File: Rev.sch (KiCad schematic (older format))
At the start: 17 parts

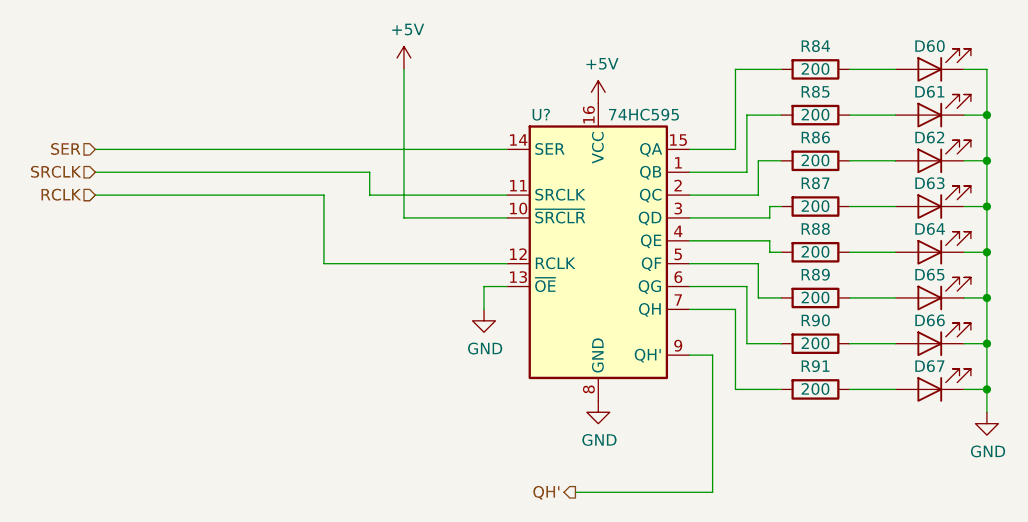
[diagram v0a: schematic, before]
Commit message: footprints; library for 7seg; start pcb layout
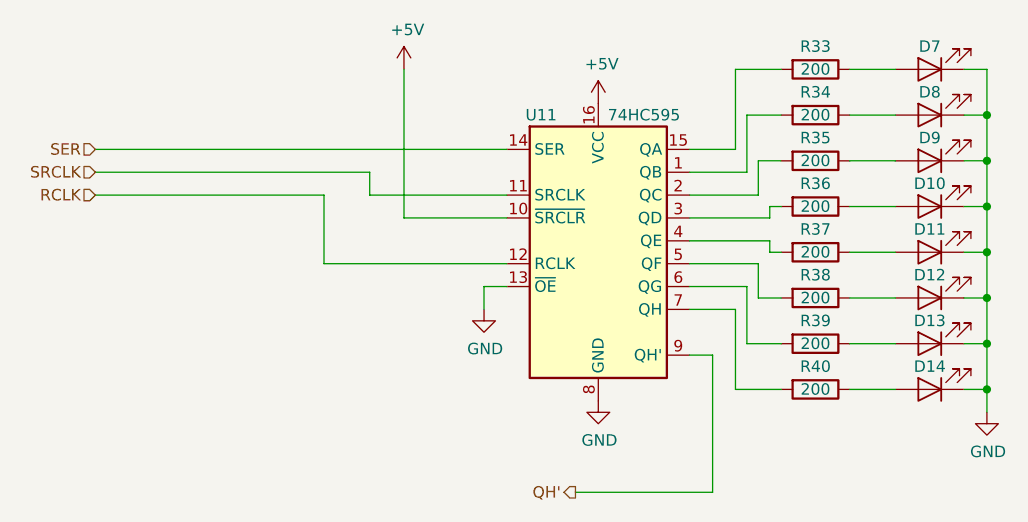
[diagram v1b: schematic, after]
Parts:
- D10: renamed from D63; footprint (none) -> LED_THT:LED_D3.0mm_Clear
- D11: renamed from D64; footprint (none) -> LED_THT:LED_D3.0mm_Clear
- D12: renamed from D65; footprint (none) -> LED_THT:LED_D3.0mm_Clear
- D13: renamed from D66; footprint (none) -> LED_THT:LED_D3.0mm_Clear
- D14: renamed from D67; footprint (none) -> LED_THT:LED_D3.0mm_Clear
- D7: renamed from D60; footprint (none) -> LED_THT:LED_D3.0mm_Clear
- D8: renamed from D61; footprint (none) -> LED_THT:LED_D3.0mm_Clear
- D9: renamed from D62; footprint (none) -> LED_THT:LED_D3.0mm_Clear
- R33: renamed from R84; footprint (none) -> Resistor_SMD:R_0603_1608Metric
- R34: renamed from R85; footprint (none) -> Resistor_SMD:R_0603_1608Metric
- R35: renamed from R86; footprint (none) -> Resistor_SMD:R_0603_1608Metric
- R36: renamed from R87; footprint (none) -> Resistor_SMD:R_0603_1608Metric
- R37: renamed from R88; footprint (none) -> Resistor_SMD:R_0603_1608Metric
- R38: renamed from R89; footprint (none) -> Resistor_SMD:R_0603_1608Metric
- R39: renamed from R90; footprint (none) -> Resistor_SMD:R_0603_1608Metric
- R40: renamed from R91; footprint (none) -> Resistor_SMD:R_0603_1608Metric
- U11: renamed from U?; footprint (none) -> Package_SO:SOIC-16_3.9x9.9mm_P1.27mm
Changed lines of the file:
@@
 $Descr A4 11693 8268
 encoding utf-8
-Sheet 7 9
+Sheet 6 9
 Title ""
 Date ""
@@
 AR Path="/61F6E690" Ref="U?"  Part="1"
 AR Path="/5FCC310D/61F6E690" Ref="U?"  Part="1"
-AR Path="/61EF75E6/61F6E690" Ref="U?"  Part="1"
-F 0 "U?" H 5450 4150 50  0000 C CNN
+AR Path="/61EF75E6/61F6E690" Ref="U11"  Part="1"
+F 0 "U11" H 5450 4150 50  0000 C CNN
 F 1 "74HC595" H 5900 4150 50  0000 C CNN
-F 2 "" H 5700 3600 50  0001 C CNN
+F 2 "Package_SO:SOIC-16_3.9x9.9mm_P1.27mm" H 5700 3600 50  0001 C CNN
 F 3 "http://www.ti.com/lit/ds/symlink/sn74hc595.pdf" H 5700 3600 50  0001 C CNN
 	1    5700 3600
@@
 AR Path="/61F6E696" Ref="R?"  Part="1"
 AR Path="/5FCC310D/61F6E696" Ref="R?"  Part="1"
-AR Path="/61EF75E6/61F6E696" Ref="R84"  Part="1"
-F 0 "R84" V 6550 2850 50  0000 C CNN
+AR Path="/61EF75E6/61F6E696" Ref="R33"  Part="1"
+F 0 "R33" V 6550 2850 50  0000 C CNN
 F 1 "200" V 6650 2850 50  0000 C CNN
-F 2 "" V 6580 2850 50  0001 C CNN
+F 2 "Resistor_SMD:R_0603_1608Metric" V 6580 2850 50  0001 C CNN
 F 3 "~" H 6650 2850 50  0001 C CNN
 	1    6650 2850
@@
 AR Path="/61F6E69C" Ref="D?"  Part="1"
 AR Path="/5FCC310D/61F6E69C" Ref="D?"  Part="1"
-AR Path="/61EF75E6/61F6E69C" Ref="D60"  Part="1"
-F 0 "D60" H 7150 2750 50  0000 C CNN
+AR Path="/61EF75E6/61F6E69C" Ref="D7"  Part="1"
+F 0 "D7" H 7150 2750 50  0000 C CNN
 F 1 "LED" H 7142 2686 50  0001 C CNN
-F 2 "" H 7150 2850 50  0001 C CNN
+F 2 "LED_THT:LED_D3.0mm_Clear" H 7150 2850 50  0001 C CNN
 F 3 "~" H 7150 2850 50  0001 C CNN
 	1    7150 2850
@@
 AR Path="/61F6E6A2" Ref="R?"  Part="1"
 AR Path="/5FCC310D/61F6E6A2" Ref="R?"  Part="1"
-AR Path="/61EF75E6/61F6E6A2" Ref="R85"  Part="1"
-F 0 "R85" V 6550 3050 50  0000 C CNN
+AR Path="/61EF75E6/61F6E6A2" Ref="R34"  Part="1"
+F 0 "R34" V 6550 3050 50  0000 C CNN
 F 1 "200" V 6650 3050 50  0000 C CNN
-F 2 "" V 6580 3050 50  0001 C CNN
+F 2 "Resistor_SMD:R_0603_1608Metric" V 6580 3050 50  0001 C CNN
 F 3 "~" H 6650 3050 50  0001 C CNN
 	1    6650 3050
@@
 AR Path="/61F6E6A8" Ref="D?"  Part="1"
 AR Path="/5FCC310D/61F6E6A8" Ref="D?"  Part="1"
-AR Path="/61EF75E6/61F6E6A8" Ref="D61"  Part="1"
-F 0 "D61" H 7150 2950 50  0000 C CNN
+AR Path="/61EF75E6/61F6E6A8" Ref="D8"  Part="1"
+F 0 "D8" H 7150 2950 50  0000 C CNN
 F 1 "LED" H 7142 2886 50  0001 C CNN
-F 2 "" H 7150 3050 50  0001 C CNN
+F 2 "LED_THT:LED_D3.0mm_Clear" H 7150 3050 50  0001 C CNN
 F 3 "~" H 7150 3050 50  0001 C CNN
 	1    7150 3050
@@
 AR Path="/61F6E6AE" Ref="R?"  Part="1"
 AR Path="/5FCC310D/61F6E6AE" Ref="R?"  Part="1"
-AR Path="/61EF75E6/61F6E6AE" Ref="R86"  Part="1"
-F 0 "R86" V 6550 3250 50  0000 C CNN
+AR Path="/61EF75E6/61F6E6AE" Ref="R35"  Part="1"
+F 0 "R35" V 6550 3250 50  0000 C CNN
 F 1 "200" V 6650 3250 50  0000 C CNN
-F 2 "" V 6580 3250 50  0001 C CNN
+F 2 "Resistor_SMD:R_0603_1608Metric" V 6580 3250 50  0001 C CNN
 F 3 "~" H 6650 3250 50  0001 C CNN
 	1    6650 3250
@@
 AR Path="/61F6E6B4" Ref="D?"  Part="1"
 AR Path="/5FCC310D/61F6E6B4" Ref="D?"  Part="1"
-AR Path="/61EF75E6/61F6E6B4" Ref="D62"  Part="1"
-F 0 "D62" H 7150 3150 50  0000 C CNN
+AR Path="/61EF75E6/61F6E6B4" Ref="D9"  Part="1"
+F 0 "D9" H 7150 3150 50  0000 C CNN
 F 1 "LED" H 7142 3086 50  0001 C CNN
-F 2 "" H 7150 3250 50  0001 C CNN
+F 2 "LED_THT:LED_D3.0mm_Clear" H 7150 3250 50  0001 C CNN
 F 3 "~" H 7150 3250 50  0001 C CNN
 	1    7150 3250
@@
 AR Path="/61F6E6BA" Ref="R?"  Part="1"
 AR Path="/5FCC310D/61F6E6BA" Ref="R?"  Part="1"
-AR Path="/61EF75E6/61F6E6BA" Ref="R87"  Part="1"
-F 0 "R87" V 6550 3450 50  0000 C CNN
+AR Path="/61EF75E6/61F6E6BA" Ref="R36"  Part="1"
+F 0 "R36" V 6550 3450 50  0000 C CNN
 F 1 "200" V 6650 3450 50  0000 C CNN
-F 2 "" V 6580 3450 50  0001 C CNN
+F 2 "Resistor_SMD:R_0603_1608Metric" V 6580 3450 50  0001 C CNN
 F 3 "~" H 6650 3450 50  0001 C CNN
 	1    6650 3450
@@
 AR Path="/61F6E6C0" Ref="D?"  Part="1"
 AR Path="/5FCC310D/61F6E6C0" Ref="D?"  Part="1"
-AR Path="/61EF75E6/61F6E6C0" Ref="D63"  Part="1"
-F 0 "D63" H 7150 3350 50  0000 C CNN
+AR Path="/61EF75E6/61F6E6C0" Ref="D10"  Part="1"
+F 0 "D10" H 7150 3350 50  0000 C CNN
 F 1 "LED" H 7142 3286 50  0001 C CNN
-F 2 "" H 7150 3450 50  0001 C CNN
+F 2 "LED_THT:LED_D3.0mm_Clear" H 7150 3450 50  0001 C CNN
 F 3 "~" H 7150 3450 50  0001 C CNN
 	1    7150 3450
@@
 AR Path="/61F6E6C6" Ref="R?"  Part="1"
 AR Path="/5FCC310D/61F6E6C6" Ref="R?"  Part="1"
-AR Path="/61EF75E6/61F6E6C6" Ref="R88"  Part="1"
-F 0 "R88" V 6550 3650 50  0000 C CNN
+AR Path="/61EF75E6/61F6E6C6" Ref="R37"  Part="1"
+F 0 "R37" V 6550 3650 50  0000 C CNN
 F 1 "200" V 6650 3650 50  0000 C CNN
-F 2 "" V 6580 3650 50  0001 C CNN
+F 2 "Resistor_SMD:R_0603_1608Metric" V 6580 3650 50  0001 C CNN
 F 3 "~" H 6650 3650 50  0001 C CNN
 	1    6650 3650
@@
 AR Path="/61F6E6CC" Ref="D?"  Part="1"
 AR Path="/5FCC310D/61F6E6CC" Ref="D?"  Part="1"
-AR Path="/61EF75E6/61F6E6CC" Ref="D64"  Part="1"
-F 0 "D64" H 7150 3550 50  0000 C CNN
+AR Path="/61EF75E6/61F6E6CC" Ref="D11"  Part="1"
+F 0 "D11" H 7150 3550 50  0000 C CNN
 F 1 "LED" H 7142 3486 50  0001 C CNN
-F 2 "" H 7150 3650 50  0001 C CNN
+F 2 "LED_THT:LED_D3.0mm_Clear" H 7150 3650 50  0001 C CNN
 F 3 "~" H 7150 3650 50  0001 C CNN
 	1    7150 3650
@@
 AR Path="/61F6E6D2" Ref="R?"  Part="1"
 AR Path="/5FCC310D/61F6E6D2" Ref="R?"  Part="1"
-AR Path="/61EF75E6/61F6E6D2" Ref="R89"  Part="1"
-F 0 "R89" V 6550 3850 50  0000 C CNN
+AR Path="/61EF75E6/61F6E6D2" Ref="R38"  Part="1"
+F 0 "R38" V 6550 3850 50  0000 C CNN
 F 1 "200" V 6650 3850 50  0000 C CNN
-F 2 "" V 6580 3850 50  0001 C CNN
+F 2 "Resistor_SMD:R_0603_1608Metric" V 6580 3850 50  0001 C CNN
 F 3 "~" H 6650 3850 50  0001 C CNN
 	1    6650 3850
@@
 AR Path="/61F6E6D8" Ref="D?"  Part="1"
 AR Path="/5FCC310D/61F6E6D8" Ref="D?"  Part="1"
-AR Path="/61EF75E6/61F6E6D8" Ref="D65"  Part="1"
-F 0 "D65" H 7150 3750 50  0000 C CNN
+AR Path="/61EF75E6/61F6E6D8" Ref="D12"  Part="1"
+F 0 "D12" H 7150 3750 50  0000 C CNN
 F 1 "LED" H 7142 3686 50  0001 C CNN
-F 2 "" H 7150 3850 50  0001 C CNN
+F 2 "LED_THT:LED_D3.0mm_Clear" H 7150 3850 50  0001 C CNN
 F 3 "~" H 7150 3850 50  0001 C CNN
 	1    7150 3850
@@
 AR Path="/61F6E6DE" Ref="R?"  Part="1"
 AR Path="/5FCC310D/61F6E6DE" Ref="R?"  Part="1"
-AR Path="/61EF75E6/61F6E6DE" Ref="R90"  Part="1"
-F 0 "R90" V 6550 4050 50  0000 C CNN
+AR Path="/61EF75E6/61F6E6DE" Ref="R39"  Part="1"
+F 0 "R39" V 6550 4050 50  0000 C CNN
 F 1 "200" V 6650 4050 50  0000 C CNN
-F 2 "" V 6580 4050 50  0001 C CNN
+F 2 "Resistor_SMD:R_0603_1608Metric" V 6580 4050 50  0001 C CNN
 F 3 "~" H 6650 4050 50  0001 C CNN
 	1    6650 4050
@@
 AR Path="/61F6E6E4" Ref="D?"  Part="1"
 AR Path="/5FCC310D/61F6E6E4" Ref="D?"  Part="1"
-AR Path="/61EF75E6/61F6E6E4" Ref="D66"  Part="1"
-F 0 "D66" H 7150 3950 50  0000 C CNN
+AR Path="/61EF75E6/61F6E6E4" Ref="D13"  Part="1"
+F 0 "D13" H 7150 3950 50  0000 C CNN
 F 1 "LED" H 7142 3886 50  0001 C CNN
-F 2 "" H 7150 4050 50  0001 C CNN
+F 2 "LED_THT:LED_D3.0mm_Clear" H 7150 4050 50  0001 C CNN
 F 3 "~" H 7150 4050 50  0001 C CNN
 	1    7150 4050
@@
 AR Path="/61F6E6EA" Ref="R?"  Part="1"
 AR Path="/5FCC310D/61F6E6EA" Ref="R?"  Part="1"
-AR Path="/61EF75E6/61F6E6EA" Ref="R91"  Part="1"
-F 0 "R91" V 6550 4250 50  0000 C CNN
+AR Path="/61EF75E6/61F6E6EA" Ref="R40"  Part="1"
+F 0 "R40" V 6550 4250 50  0000 C CNN
 F 1 "200" V 6650 4250 50  0000 C CNN
-F 2 "" V 6580 4250 50  0001 C CNN
+F 2 "Resistor_SMD:R_0603_1608Metric" V 6580 4250 50  0001 C CNN
 F 3 "~" H 6650 4250 50  0001 C CNN
 	1    6650 4250
@@
 AR Path="/61F6E6F0" Ref="D?"  Part="1"
 AR Path="/5FCC310D/61F6E6F0" Ref="D?"  Part="1"
-AR Path="/61EF75E6/61F6E6F0" Ref="D67"  Part="1"
-F 0 "D67" H 7150 4150 50  0000 C CNN
+AR Path="/61EF75E6/61F6E6F0" Ref="D14"  Part="1"
+F 0 "D14" H 7150 4150 50  0000 C CNN
 F 1 "LED" H 7150 4150 50  0001 C CNN
-F 2 "" H 7150 4250 50  0001 C CNN
+F 2 "LED_THT:LED_D3.0mm_Clear" H 7150 4250 50  0001 C CNN
 F 3 "~" H 7150 4250 50  0001 C CNN
 	1    7150 4250
@@
 AR Path="/61F6E72D" Ref="#PWR?"  Part="1"
 AR Path="/5FCC310D/61F6E72D" Ref="#PWR?"  Part="1"
-AR Path="/61EF75E6/61F6E72D" Ref="#PWR?"  Part="1"
-F 0 "#PWR?" H 7400 4100 50  0001 C CNN
+AR Path="/61EF75E6/61F6E72D" Ref="#PWR044"  Part="1"
+F 0 "#PWR044" H 7400 4100 50  0001 C CNN
 F 1 "GND" H 7405 4177 50  0000 C CNN
 F 2 "" H 7400 4350 50  0001 C CNN
@@
 AR Path="/61F6E735" Ref="#PWR?"  Part="1"
 AR Path="/5FCC310D/61F6E735" Ref="#PWR?"  Part="1"
-AR Path="/61EF75E6/61F6E735" Ref="#PWR?"  Part="1"
-F 0 "#PWR?" H 5700 2850 50  0001 C CNN
+AR Path="/61EF75E6/61F6E735" Ref="#PWR042"  Part="1"
+F 0 "#PWR042" H 5700 2850 50  0001 C CNN
 F 1 "+5V" H 5715 3173 50  0000 C CNN
 F 2 "" H 5700 3000 50  0001 C CNN
@@
 AR Path="/61F6E73B" Ref="#PWR?"  Part="1"
 AR Path="/5FCC310D/61F6E73B" Ref="#PWR?"  Part="1"
-AR Path="/61EF75E6/61F6E73B" Ref="#PWR?"  Part="1"
-F 0 "#PWR?" H 5700 4050 50  0001 C CNN
+AR Path="/61EF75E6/61F6E73B" Ref="#PWR043"  Part="1"
+F 0 "#PWR043" H 5700 4050 50  0001 C CNN
 F 1 "GND" H 5705 4127 50  0000 C CNN
 F 2 "" H 5700 4300 50  0001 C CNN
@@
 AR Path="/61F6E741" Ref="#PWR?"  Part="1"
 AR Path="/5FCC310D/61F6E741" Ref="#PWR?"  Part="1"
-AR Path="/61EF75E6/61F6E741" Ref="#PWR?"  Part="1"
-F 0 "#PWR?" H 5200 3650 50  0001 C CNN
+AR Path="/61EF75E6/61F6E741" Ref="#PWR041"  Part="1"
+F 0 "#PWR041" H 5200 3650 50  0001 C CNN
 F 1 "GND" H 5205 3727 50  0000 C CNN
 F 2 "" H 5200 3900 50  0001 C CNN
@@
 AR Path="/61F6E74D" Ref="#PWR?"  Part="1"
 AR Path="/5FCC310D/61F6E74D" Ref="#PWR?"  Part="1"
-AR Path="/61EF75E6/61F6E74D" Ref="#PWR?"  Part="1"
-F 0 "#PWR?" H 4850 2700 50  0001 C CNN
+AR Path="/61EF75E6/61F6E74D" Ref="#PWR040"  Part="1"
+F 0 "#PWR040" H 4850 2700 50  0001 C CNN
 F 1 "+5V" H 4865 3023 50  0000 C CNN
 F 2 "" H 4850 2850 50  0001 C CNN
